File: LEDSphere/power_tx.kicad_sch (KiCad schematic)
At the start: 67 parts, among them J1 USB_C_Receptacle_USB2.0, M1 Motor_DC, Q1 CSD18540Q5B, Q2 CSD18540Q5B, Q3 BSS138, Q4 BSS138, Q5 BSS138, Q6 BSS138, Q7 BSS138, Q8 BSS138, SW3 SW_DIP_x03, U10 HT7550-1-SOT89, U11 CH224K, U7 4017, U8 TPS54302

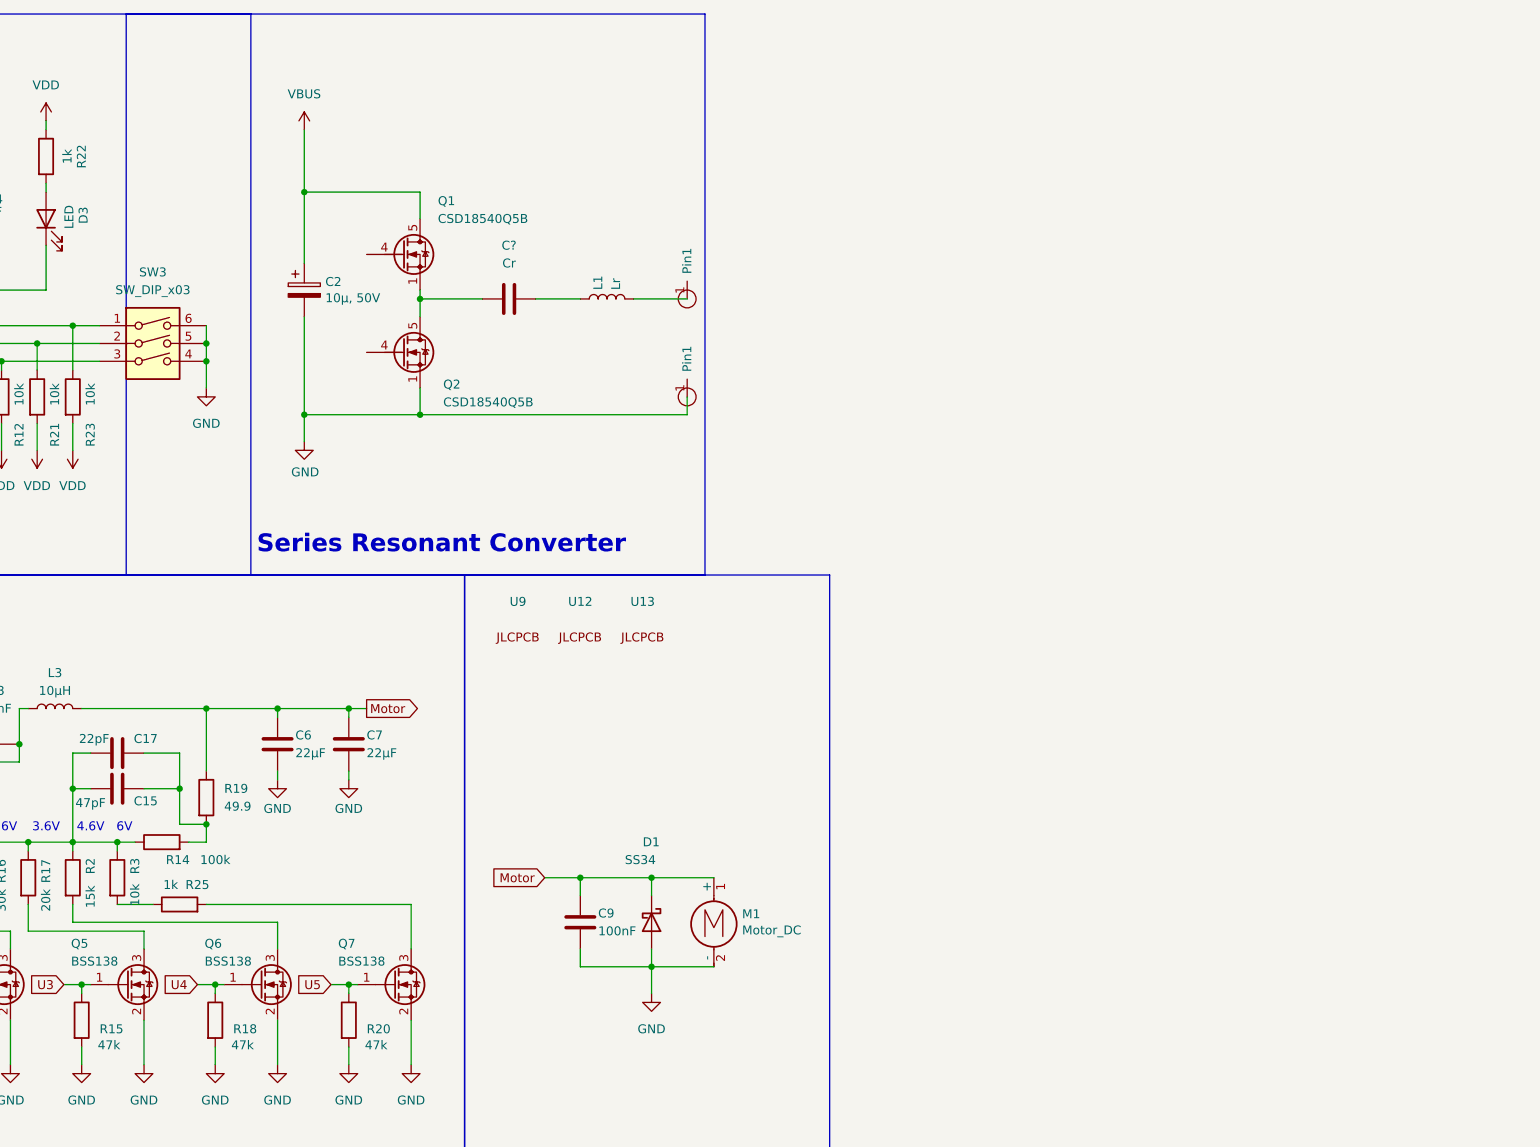
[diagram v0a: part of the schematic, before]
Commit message: started routing drivers, power mosfets
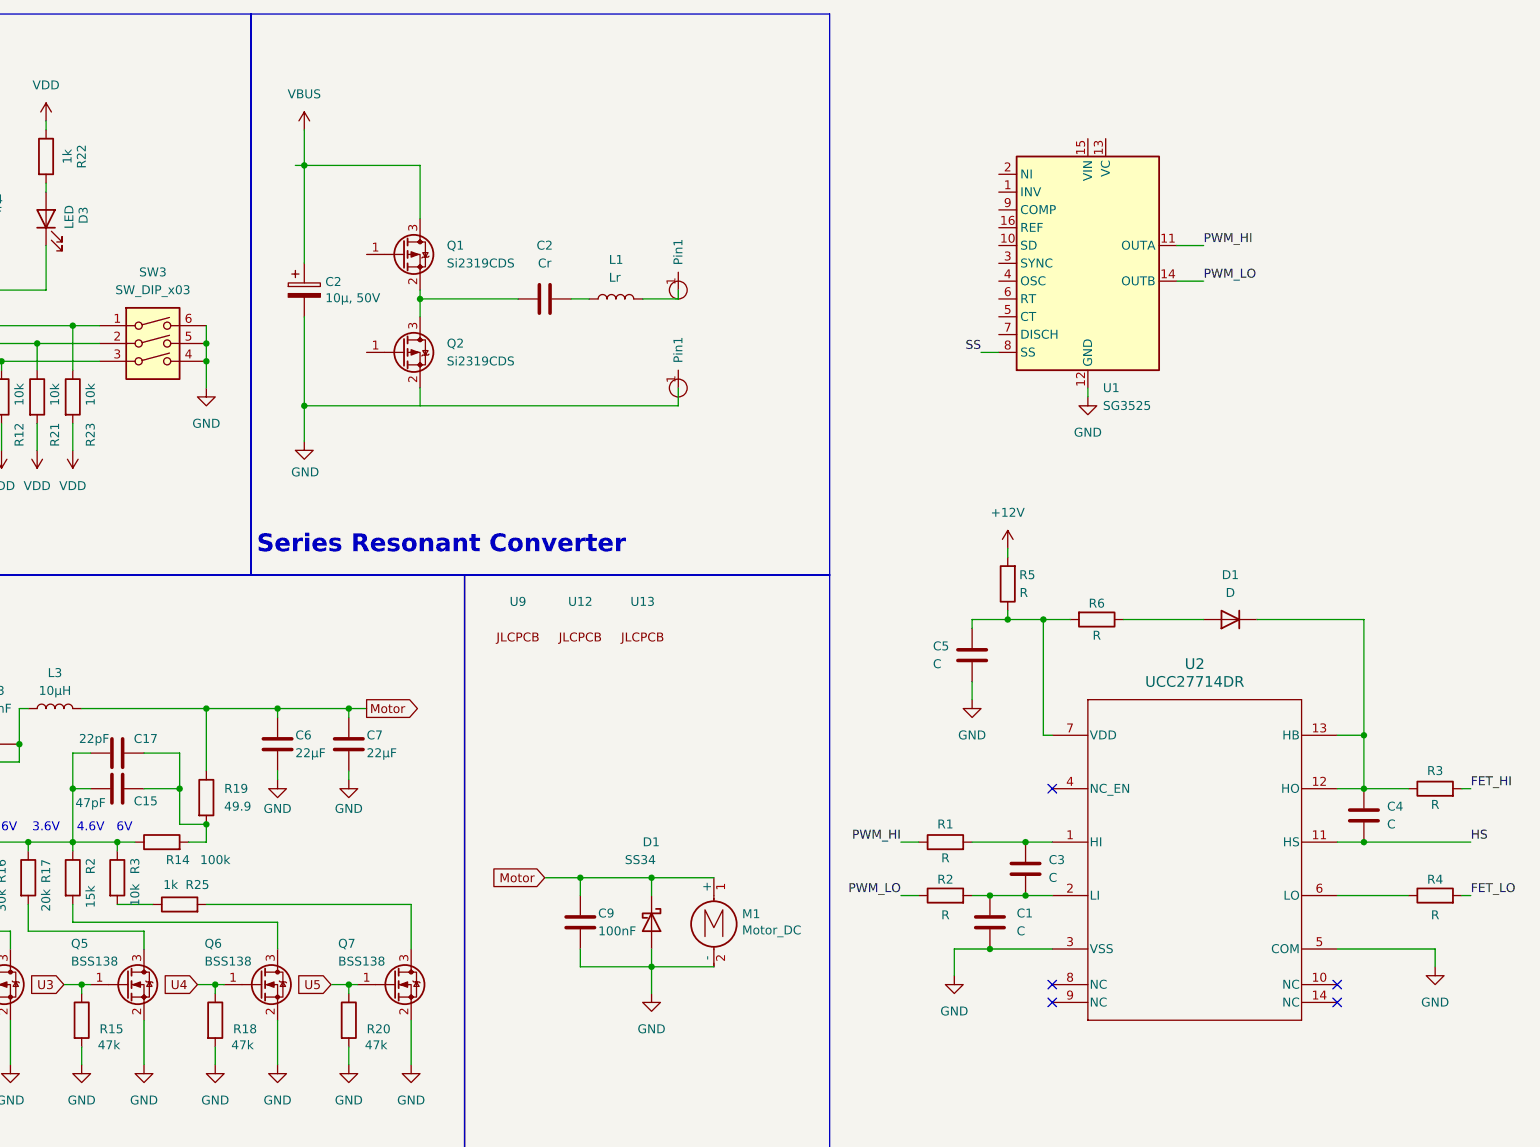
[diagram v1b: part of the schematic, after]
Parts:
- removed Q1, Q2: CSD18540Q5B, Package_TO_SOT_SMD:TDSON-8-1, symbol Transistor_FET:CSD18540Q5B
- added C1, C3, C4, C5: C, symbol Device:C
- added D1: D, symbol Device:D
- added Q1, Q2: Si2319CDS, Package_TO_SOT_SMD:SOT-23, symbol Transistor_FET:Si2319CDS
- added R1, R2, R3, R4, R5, R6: R, symbol Device:R
- added U1: SG3525, symbol Regulator_Controller:SG3525
- added U2: UCC27714DR, D0014A_N, symbol UCC27714:UCC27714DR
- gave numbers to parts that had none: 3
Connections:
- net GND: now also C1.2, C5.2, U1.12 (GND), U2.3 (VSS), U2.5 (COM)
- net VBUS: now also Q1.3 (D)
- net at C2.1: now also Q1.2 (S), Q2.3 (D)
- new net: C3.1, R1.2, U2.1 (HI)
- new net: C5.1, R5.1, R6.2, U2.7 (VDD)
- new net: C4.1, D1.1 (K), R3.1, U2.12 (HO), U2.13 (HB)
- new net: C1.1, C3.2, R2.2, U2.2 (LI)
- new net: R4.1, U2.6 (LO)
- new net: D1.2 (A), R6.1
- new net +12V: R5.2
- new net FET_HI: R3.2
- new net FET_LO: R4.2
- new net HS: C4.2, U2.11 (HS)
- new net PWM_HI: R1.1, U1.11 (OUTA)
- new net PWM_LO: R2.1, U1.14 (OUTB)
- new net SS: U1.8 (SS)
- no-connect marks 11 -> 16
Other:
- moved on the sheet: C2, L1

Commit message: finished usb-c power delivery aspect - started pwm generator sch
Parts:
- removed R12: 10k, Resistor_SMD:R_0402_1005Metric, symbol Device:R
- removed SW3: SW_DIP_x03, Button_Switch_SMD:SW_DIP_SPSTx03_Slide_9.78x9.8mm_W8.61mm_P2.54mm, symbol Switch:SW_DIP_x03
- removed U10: HT7550-1-SOT89, Package_TO_SOT_SMD:SOT-89-3, symbol Regulator_Linear:HT75xx-1-SOT89
- removed U11: CH224K, Package_SO:SSOP-10-1EP_3.9x4.9mm_P1mm_EP2.1x3.3mm, symbol Interface_USB:CH224K
- added D2: LED, symbol Device:LED
- added R26, R27: R, symbol Device:R
- added RV1: PWM_ADJ, symbol Device:R_Potentiometer_Trim
- added RV2: FRQ_ADJ, symbol Device:R_Potentiometer_Trim
- added U4: CH221K, Package_TO_SOT_SMD:SOT-23-6, symbol Interface_USB:CH221K
- C12: value 10µF -> C; footprint Capacitor_SMD:C_1206_3216Metric -> (none); LCSC C13585 -> (none)
- C16: value 100nF -> C; footprint Capacitor_SMD:C_0603_1608Metric -> (none); LCSC C14663 -> (none)
- R10: value 10k -> 47k
- R21, R23: value 10k -> 5.1k
- SW1, SW2, U12, U13, U9: value ~ -> (none)
- renumbered C2 to C?, U7 to U?, U8 to U?
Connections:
- net +12V: now also C10.2, C11.1, C2.1, C4.1, C5.1, J1.A4 (VBUS), J1.A9 (VBUS), J1.B4 (VBUS), J1.B9 (VBUS), Q1.3 (D), R11.1, R22.1, R4.1, R6.1, SW2.4, SW2.6, U7.16 (VDD), U8.3 (VIN)
- net +5V: no longer C12.1, C16.1, R4.1, R6.1, SW2.4, SW2.6, U7.16 (VDD)
- net CC1: now also R21.1, U4.4 (CC1)
- net CC2: now also R23.1, U4.5 (CC2)
- net GND: now also Q2.2 (S), R21.2, R23.2, D2.1 (K), RV1.3, RV2.3, U4.2 (GND)
- net at D3.1 (K): now also U4.3 (~{PG})
- net at R10.2: now also U4.6 (CFG)
- net at U1.1 (INV): now also U1.9 (COMP)
- net at U1.13 (VC): now also U1.15 (VIN), R26.2
- net at U1.16 (REF): now also RV1.1
- net at U1.2 (NI): now also RV1.2
- net at U1.5 (CT): now also C12.1, U1.7 (DISCH)
- net at U1.6 (RT): now also R27.1
- net SS: no longer names the net of U1.8 (SS)
- net SS: now also C16.1
- removed net VBUS: C10.2, C11.1, C2.1, C4.1, C5.1, J1.A4 (VBUS), J1.A9 (VBUS), J1.B4 (VBUS), J1.B9 (VBUS), Q1.3 (D), R10.1, R11.1, U8.3 (VIN)
- removed net VDD: C14.1, R11.2, R21.2, R22.1, R23.2
- new net: R27.2, RV2.1, RV2.2
- new net: C14.1, R10.1, R11.2, U4.1 (VDD)
- new net: D2.2 (A), R26.1
- no-connect marks 16 -> 19
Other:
- note removed: "+5V regulator"
- moved on the sheet: C1, C14, C2, C3, C4, C5, C?, D1, D3, L1, Q1, Q2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

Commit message: first draft of power board
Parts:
- removed C1: C, symbol Device:C
- removed RV1: PWM_ADJ, symbol Device:R_Potentiometer_Trim
- added C13: 10nF, symbol Device:C
- added C16, C18: 1uF, symbol Device:C
- added C21: C, symbol Device:C
- added R24, R32, R33: 10k, symbol Device:R
- added R25: 22R, symbol Device:R
- C11: renamed from C12; value C -> 1nF
- C15: renamed from C16; value C -> 1uF
- C23: renamed from C?; value Cr -> 330nF
- L2: renamed from L1; value Lr -> 6uF
- R23: renamed from R27; value R -> 1k
- gave numbers to parts that had none: 2
- renumbered C3 to C1, C15 to C10, C6 to C12, C7 to C14, C9 to C17, C5 to C19, C10 to C2, C2 to C20, C3 to C22, C4 to C24, C8 to C3, C11 to C4, C14 to C5, C4 to C6, C5 to C7, C13 to C8, C17 to C9, D3 to D1, D1 to D2, D2 to D3, D1 to D4, L3 to L1, Q8 to Q1, Q3 to Q2, Q4 to Q3, Q5 to Q4, Q6 to Q5, Q7 to Q6, Q1 to Q7, Q2 to Q8, R4 to R1, R7 to R10, R22 to R11, R13 to R12, R9 to R13, R16 to R14, R17 to R15, R2 to R16, R15 to R17, R3 to R18, R14 to R19, R5 to R2, R25 to R20, R19 to R21, R18 to R22, R20 to R26, R26 to R27, R1 to R28, R2 to R29, R8 to R3, R5 to R30, R6 to R31, R3 to R34, R4 to R35, R23 to R4, R21 to R5, R24 to R6, R11 to R7, R6 to R8, R10 to R9, RV2 to RV1, U7 to U1, U4 to U2, U8 to U3, U1 to U4, U9 to U5, U12 to U6, U13 to U7, U2 to U8
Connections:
- net FET_HI: now also Q7.1 (G), R32.2
- net FET_LO: now also Q8.1 (G), R33.2
- net GND: now also C22.2, U4.1 (INV), C13.1, C16.2, C18.2, C21.2, R24.2, R33.1
- net HS: now also C23.1, Q7.2 (S), Q8.3 (D), R32.1
- net at C24.1, D4.1 (K), U8.13 (HB): no longer R34.1, U8.12 (HO)
- net at R29.2, U8.2 (LI): now also C21.1; no longer C22.2
- net at C11.1, U4.5 (CT): now also R25.2; no longer U4.7 (DISCH)
- net at D3.2 (A): now also R27.2; no longer R27.1
- net at U4.16 (REF): now also U4.2 (NI)
- net at U4.13 (VC), U4.15 (VIN): now also R27.1, C16.1, C18.1; no longer R27.2
- net at U4.9 (COMP): now also C13.2; no longer U4.1 (INV)
- net at U4.10 (SD): now also R24.1
- net OSC: now reaches U4.4 (OSC)
- new net: R34.1, U8.12 (HO)
- new net: R25.1, U4.7 (DISCH)
- no-connect marks 19 -> 17
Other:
- moved on the sheet: C11, C22, C23, D3, L2, R23, R27

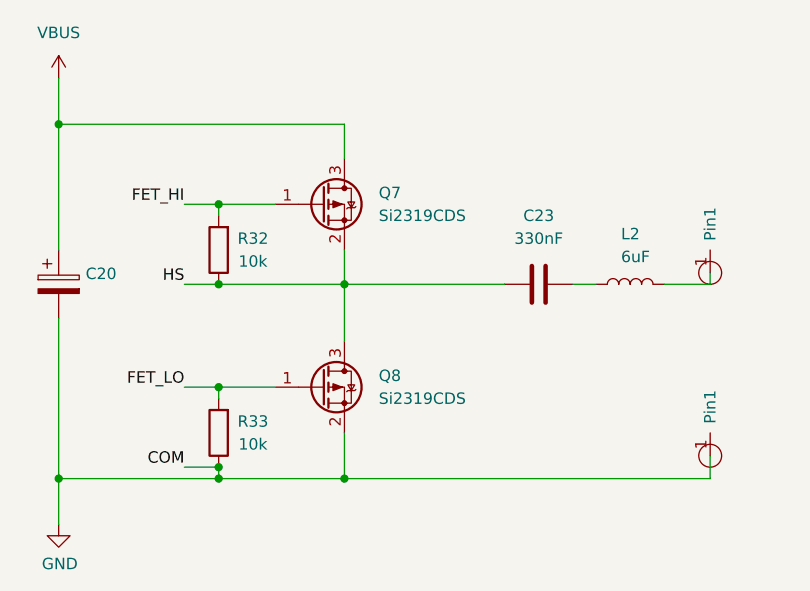
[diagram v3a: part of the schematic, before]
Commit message: edit power mosfet orientation
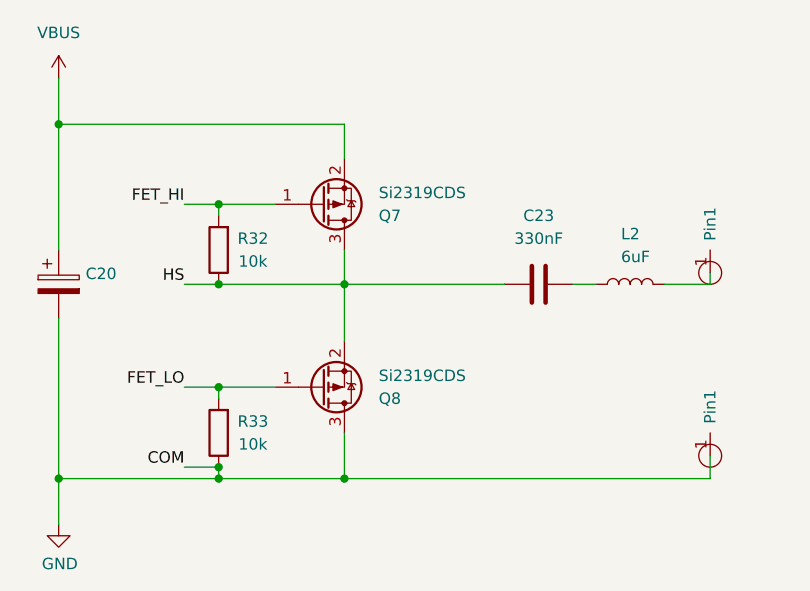
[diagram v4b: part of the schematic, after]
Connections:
- net +12V: now also Q7.2 (S); no longer Q7.3 (D)
- net GND: now also Q8.3 (D); no longer Q8.2 (S)
- net HS: now also Q7.3 (D), Q8.2 (S); no longer Q7.2 (S), Q8.3 (D)
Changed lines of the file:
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@@
 		(lib_id "Transistor_FET:Si2319CDS")
 		(at 345.44 151.13 0)
+		(mirror x)
 		(unit 1)
 		(body_style 1)
@@
 		(in_pos_files yes)
 		(dnp no)
-		(fields_autoplaced yes)
 		(property "Reference" "Q8"
-			(at 351.79 149.8599 0)
+			(at 351.79 152.4001 0)
 			(show_name no)
 			(do_not_autoplace no)
@@
 		)
 		(property "Value" "Si2319CDS"
-			(at 351.79 152.3999 0)
+			(at 351.79 149.8601 0)
 			(show_name no)
 			(do_not_autoplace no)
@@
 		)
 		(property "Footprint" "Package_TO_SOT_SMD:SOT-23"
-			(at 350.52 153.035 0)
+			(at 350.52 149.225 0)
 			(hide yes)
 			(show_name no)
@@
 		)
 		(property "Datasheet" "http://www.vishay.com/docs/66709/si2319cd.pdf"
-			(at 350.52 154.94 0)
+			(at 350.52 147.32 0)
 			(hide yes)
 			(show_name no)
@@
 		(lib_id "Transistor_FET:Si2319CDS")
 		(at 345.44 130.81 0)
+		(mirror x)
 		(unit 1)
 		(body_style 1)
@@
 		(in_pos_files yes)
 		(dnp no)
-		(fields_autoplaced yes)
 		(property "Reference" "Q7"
-			(at 351.79 129.5399 0)
+			(at 351.79 132.0801 0)
 			(show_name no)
 			(do_not_autoplace no)
@@
 		)
 		(property "Value" "Si2319CDS"
-			(at 351.79 132.0799 0)
+			(at 351.79 129.5401 0)
 			(show_name no)
 			(do_not_autoplace no)
@@
 		)
 		(property "Footprint" "Package_TO_SOT_SMD:SOT-23"
-			(at 350.52 132.715 0)
+			(at 350.52 128.905 0)
 			(hide yes)
 			(show_name no)
@@
 		)
 		(property "Datasheet" "http://www.vishay.com/docs/66709/si2319cd.pdf"
-			(at 350.52 134.62 0)
+			(at 350.52 127 0)
 			(hide yes)
 			(show_name no)
